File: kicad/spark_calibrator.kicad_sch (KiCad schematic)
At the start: 18 parts, among them J1 PWM, J2 Coil+, J3 Coil-, J4 12V IN, Q1 BS170, Q2 IRFP460PBF, U1 4N28

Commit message: aestetic updates
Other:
- note added: "coil driver"
- note added: "digital"
- note added: "power input"
- company: (none) -> Author: felhub
- title: (none) -> spark_calibrator
- moved on the sheet: C1, C2, D1, D2, J1, J2, J3, J4, Q1, Q2, R1, R2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

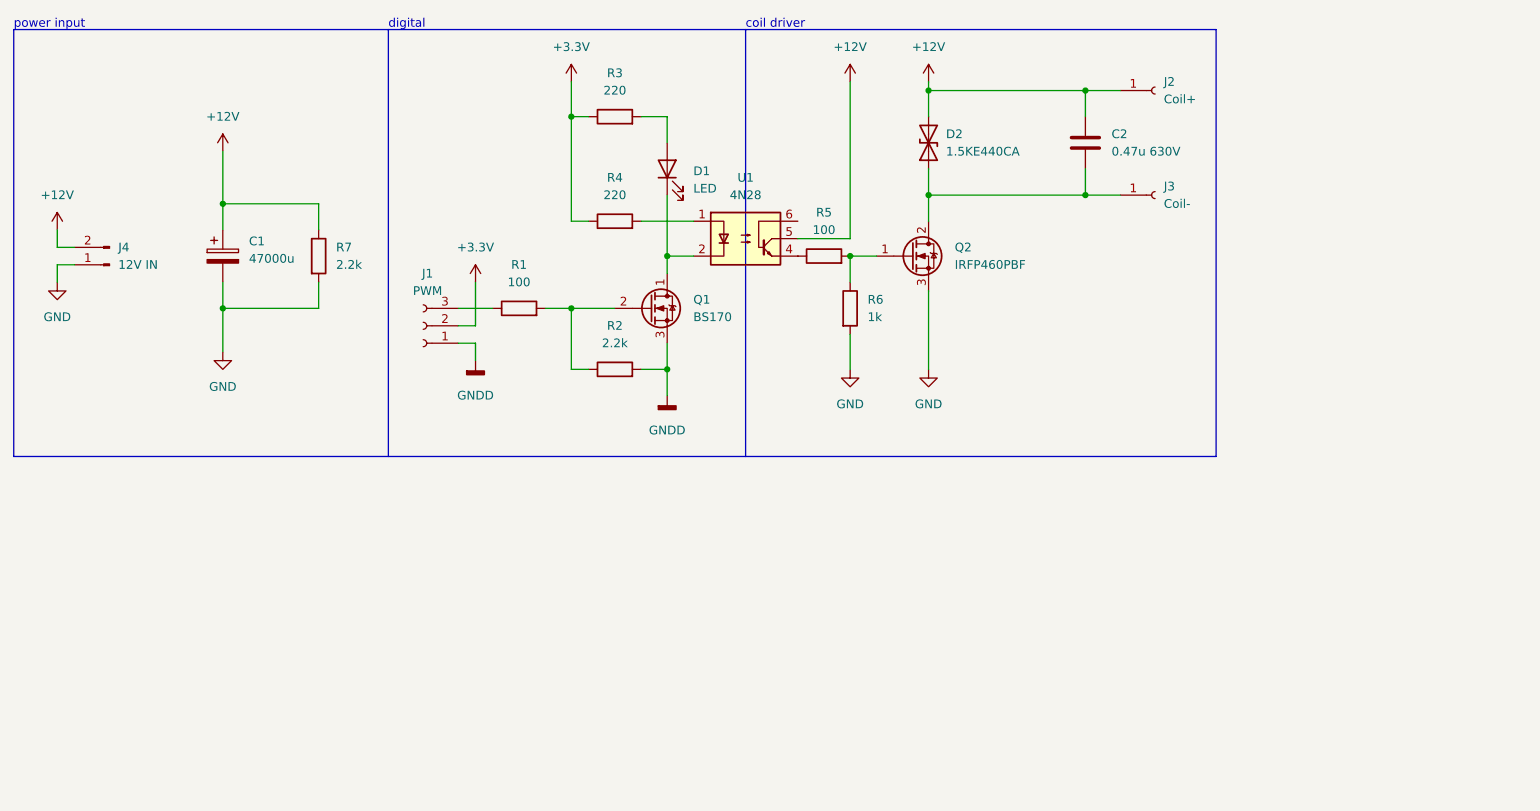
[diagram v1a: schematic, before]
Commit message: faster off switching
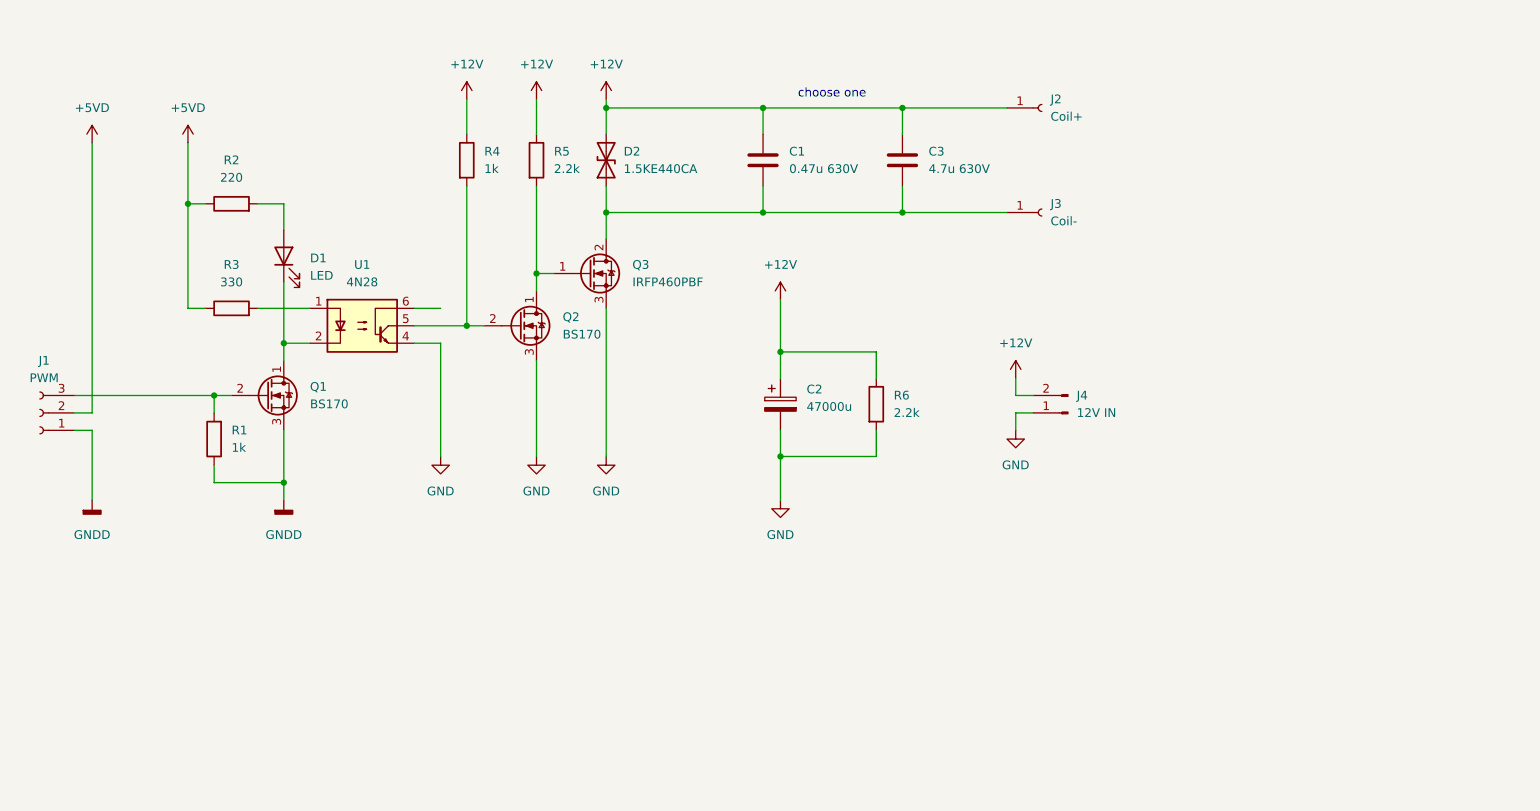
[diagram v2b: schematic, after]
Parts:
- removed R2: 2.2k, Resistor_THT:R_Axial_DIN0207_L6.3mm_D2.5mm_P10.16mm_Horizontal, symbol Device:R
- added C3: 4.7u 630V, Capacitor_THT:C_Rect_L31.5mm_W17.0mm_P27.50mm_MKS4, symbol Device:C
- added Q2: BS170, Package_TO_SOT_THT:TO-92_Inline, symbol Transistor_FET:BS170
- R1: value 100 -> 1k
- R3: renamed from R4; value 220 -> 330
- R5: value 100 -> 2.2k
- renumbered C2 to C1, C1 to C2, Q2 to Q3, R3 to R2, R6 to R4, R7 to R6
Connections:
- net +12V: now also R4.1, R5.1, C3.1; no longer U1.5
- net GND: now also U1.4, Q2.3 (S); no longer R4.2
- net GNDD: now also R1.1
- net at C1.2, D2.1 (A1), J3.1 (Pin_1)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: now also C3.2
- net at Q1.2 (G), R1.2: now also J1.3 (Pin_3)
- net at Q3.1 (G), R5.2: now also Q2.1 (D); no longer R4.1
- net +3V3 renamed +5VD
- new net: Q2.2 (G), R4.2, U1.5
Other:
- note added: "choose one"
- note removed: "coil driver"
- note removed: "digital"
- note removed: "power input"
- moved on the sheet: C1, C2, D1, D2, J1, J2, J3, J4, Q1, Q3, R2, R3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

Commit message: R4 to 2.2k
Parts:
- R4: value 1k -> 2.2k
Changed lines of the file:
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@@
       (effects (font (size 1.27 1.27)) (justify left))
     )
-    (property "Value" "1k" (id 1) (at 86.36 43.1799 0)
+    (property "Value" "2.2k" (id 1) (at 86.36 43.1799 0)
       (effects (font (size 1.27 1.27)) (justify left))
     )
@@
     )
     (path "/cfe32bab-90a4-46f8-a9e0-ccd961990a3d"
-      (reference "R4") (unit 1) (value "1k") (footprint "Resistor_THT:R_Axial_DIN0207_L6.3mm_D2.5mm_P10.16mm_Horizontal")
+      (reference "R4") (unit 1) (value "2.2k") (footprint "Resistor_THT:R_Axial_DIN0207_L6.3mm_D2.5mm_P10.16mm_Horizontal")
     )
     (path "/0d19d170-1684-4368-99df-1810e10780f8"
